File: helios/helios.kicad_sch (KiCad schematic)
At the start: 1 part

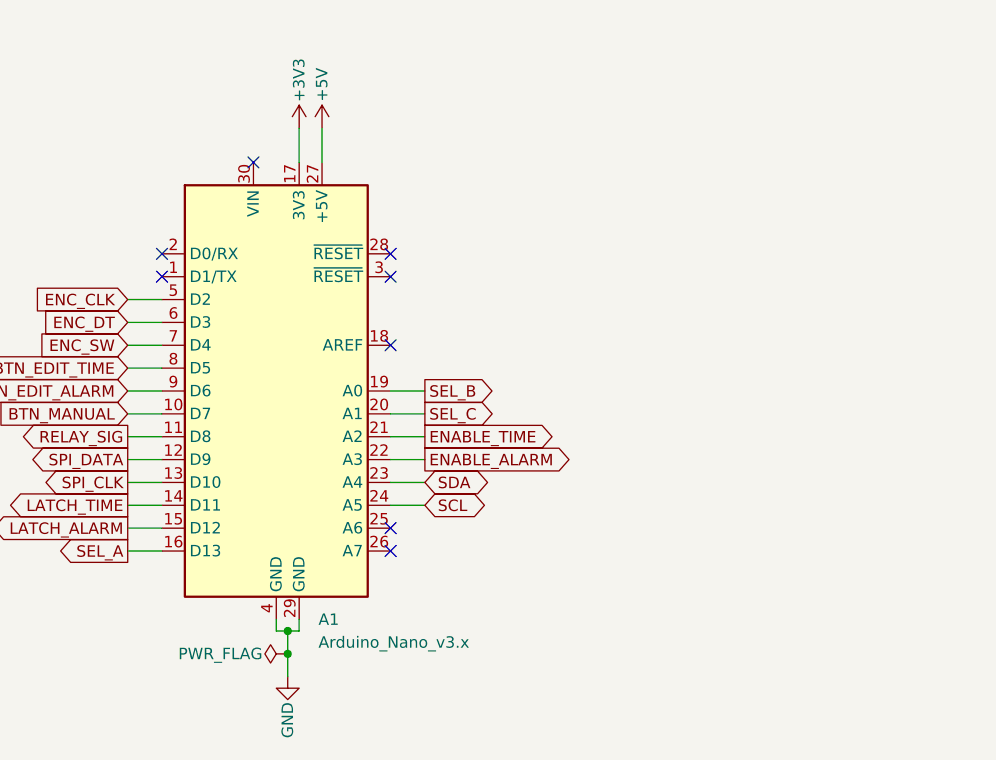
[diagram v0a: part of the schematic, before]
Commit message: finish PCB + rename project
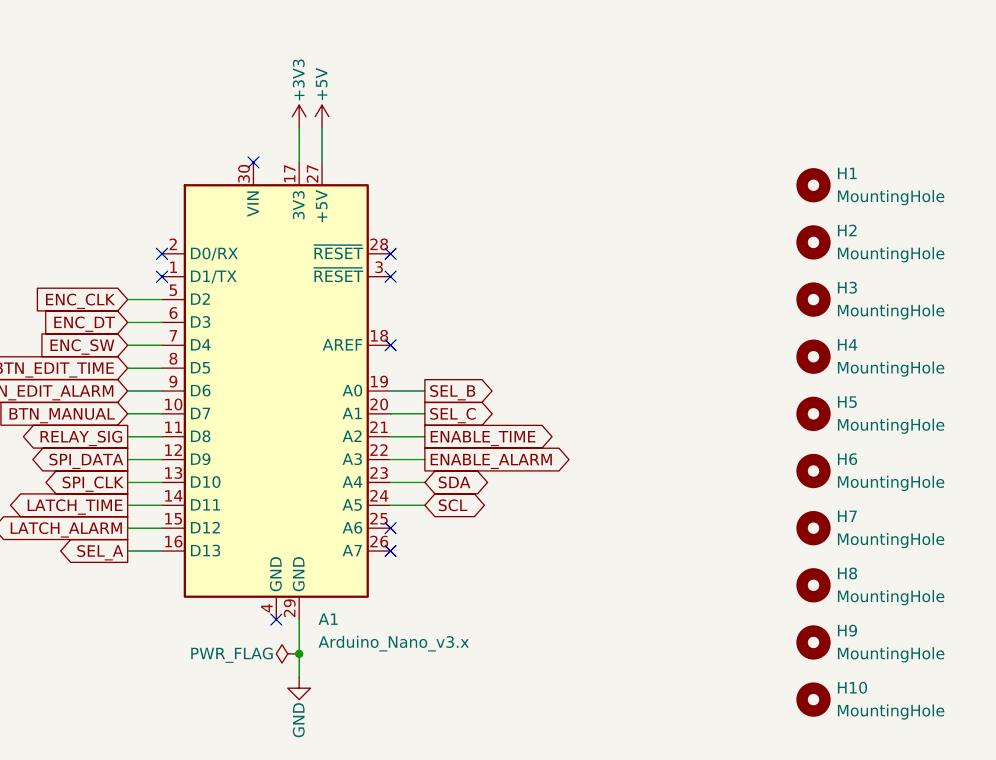
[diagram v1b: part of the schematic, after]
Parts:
- added H1, H10, H2, H3, H4, H9: MountingHole, MountingHole:MountingHole_3.2mm_M3, symbol Mechanical:MountingHole
- added H5: MountingHole, Relay_THT:Relay_Module_5V_Mounting, symbol Mechanical:MountingHole
- added H6, H7, H8: MountingHole, symbol Mechanical:MountingHole
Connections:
- net GND: no longer A1.4 (GND)
- no-connect marks 8 -> 9
